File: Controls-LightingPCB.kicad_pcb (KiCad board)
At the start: 2 copper layers, 73.9 x 98.8 mm, 92 parts, among them J1 MinionConn, J10 INTERNAL_RIGHTBLINK, J11 INTERNAL_LEFTBLINK, J12 EXTERNAL_RIGHTBLINK, J13 EXTERNAL_HDLT, J14 EXTERNAL_BRAKELIGHT, J2 12VPWRCONN, J3 CRUZ_ST_INDICATOR_33v, J4 CRUZ_EN_INDICATOR_33v, J5 REGEN_INDICATOR_33v, J6 NEU_INDICATOR_33v, J7 FOR_INDICATOR_33v, J8 REV_INDICATOR_33v, J9 EXTERNAL_LEFTBLINK, Q1 2N7000, Q2 2N7000, Q3 2N7000, Q4 2N7000, Q5 2N7000, SW1 CRUISE_SET, SW2 CRUISE_ENABLE, SW3 F/R_SW, SW4 REGEN_SW, SW5 TURN_SIGNAL_SW, U1 NCP1117-3.3_SOT223

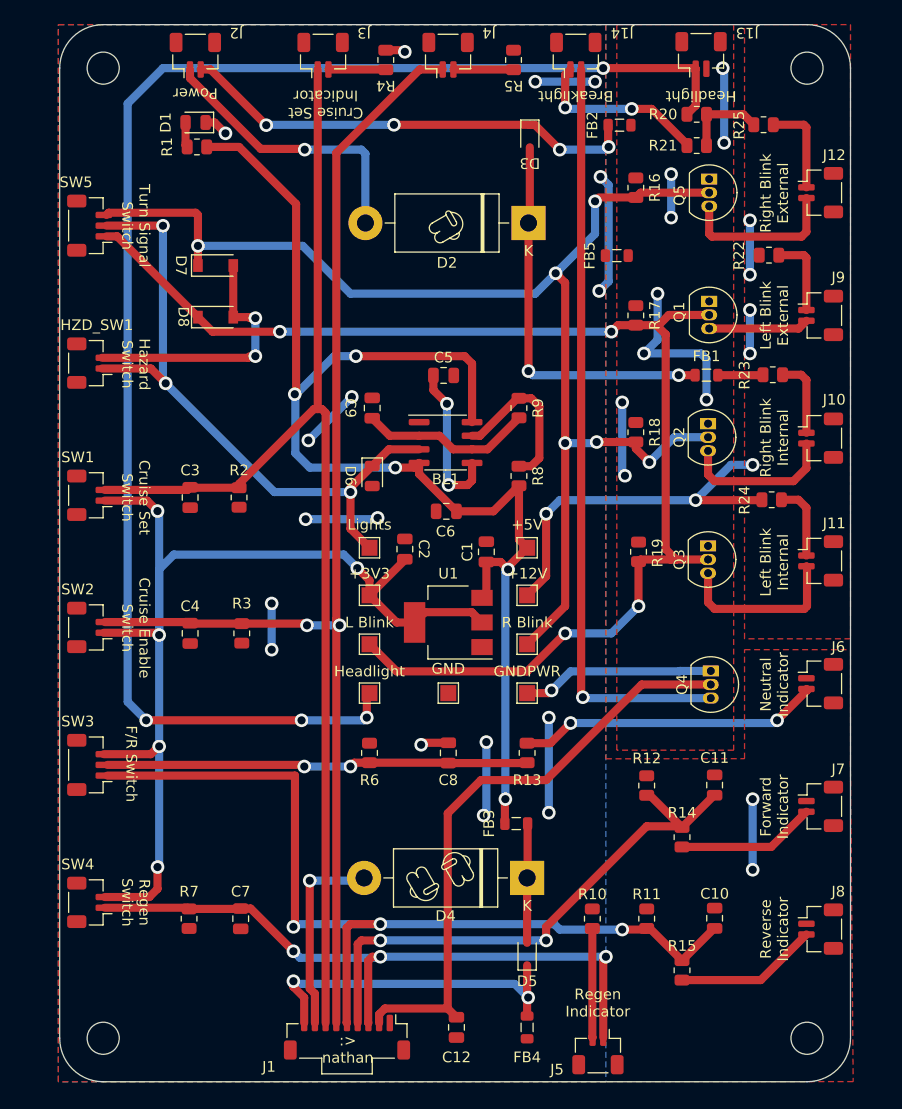
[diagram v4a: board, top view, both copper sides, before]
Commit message: Changed to SMD mosfets
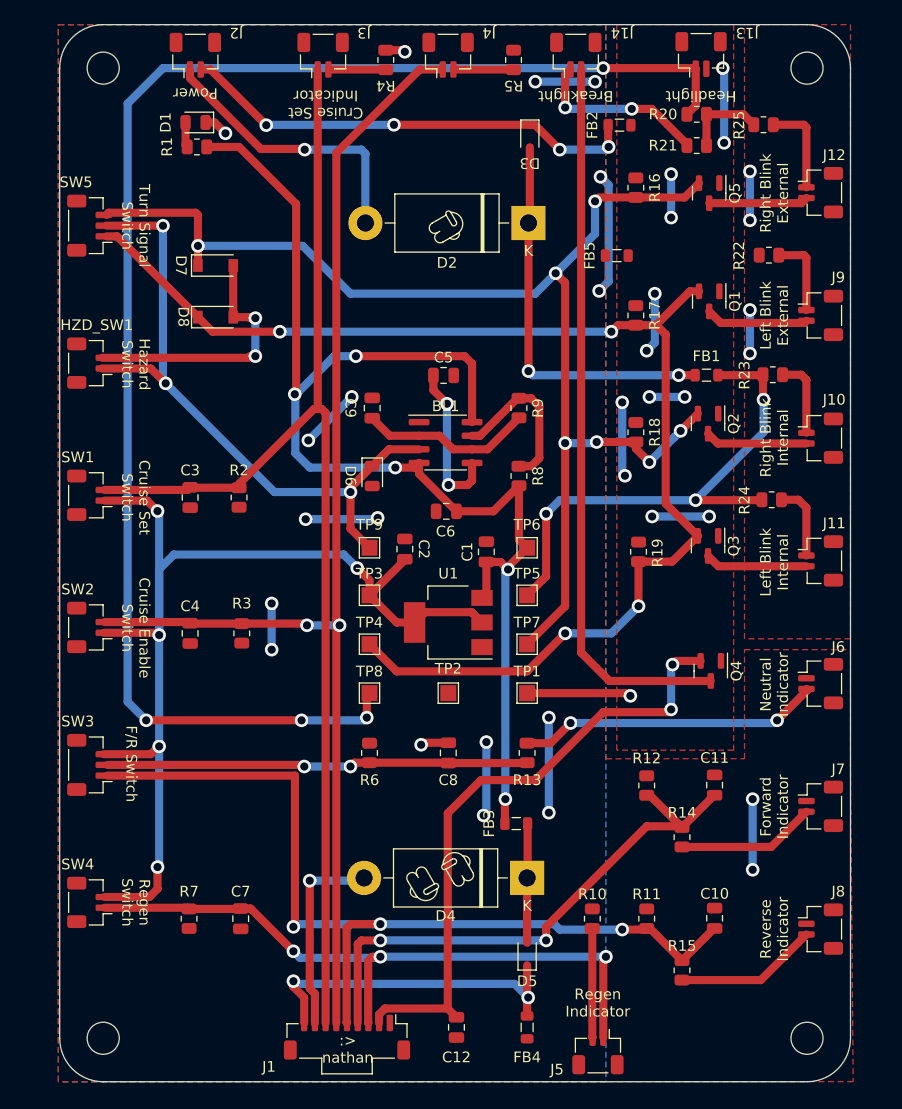
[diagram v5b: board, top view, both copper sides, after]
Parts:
- Q1, Q2, Q3, Q4, Q5: footprint Package_TO_SOT_THT:TO-92_Inline -> Package_TO_SOT_SMD:SOT-23
- TP4: renamed from L Blink
- TP7: renamed from R Blink
- moved Q5 1.31 mm to (168.7, 59.7)
- renumbered GNDPWR to TP1, GND to TP2, +3V3 to TP3, +12V to TP5, +5V to TP6, Headlight to TP8, Lights to TP9
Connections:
- net +3V3 renamed +3.3V
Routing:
- net GNDPWR: track 52.1 -> 42.1 mm, vias 10 -> 13
- net +12V: track 56.8 -> 64.0 mm
- net Net-(J11-Pad2): track 16.1 -> 9.59 mm
- net Net-(J12-Pad2): track 15.1 -> 9.29 mm
- net Net-(J10-Pad2): track 14.5 -> 9.57 mm
- net Net-(J14-Pad2): track 70.7 -> 67.7 mm, vias 1 -> 0
- net /BRAKELIGHT: track 56.4 -> 58.2 mm, vias 0 -> 2
- net /LEFT_BLINK: track 122.7 -> 121.4 mm
- net /RIGHT_BLINK: track 120.3 -> 119.5 mm, vias 6 -> 7

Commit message: updated board
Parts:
- added .: LOGO, UTSVT_Special:kevin, B.Cu at (135.9, 80.9)
- L Blink: renamed from TP4
- R Blink: renamed from TP7
- moved R20 6.01 mm to (162.3, 49.3)
- renumbered TP5 to +12V, TP3 to +3.3V, TP6 to +5V, TP2 to GND, TP1 to GNDPWR, TP8 to Headlights, TP9 to LighsCLK
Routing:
- net GNDPWR: track 42.1 -> 57.5 mm, vias 13 -> 12
- net +12V: track 64.0 -> 70.5 mm
- net Net-(BL1-Pad5): track 14.8 -> 16.4 mm
- net /HEADLIGHT_SW: track 140.6 -> 140.0 mm

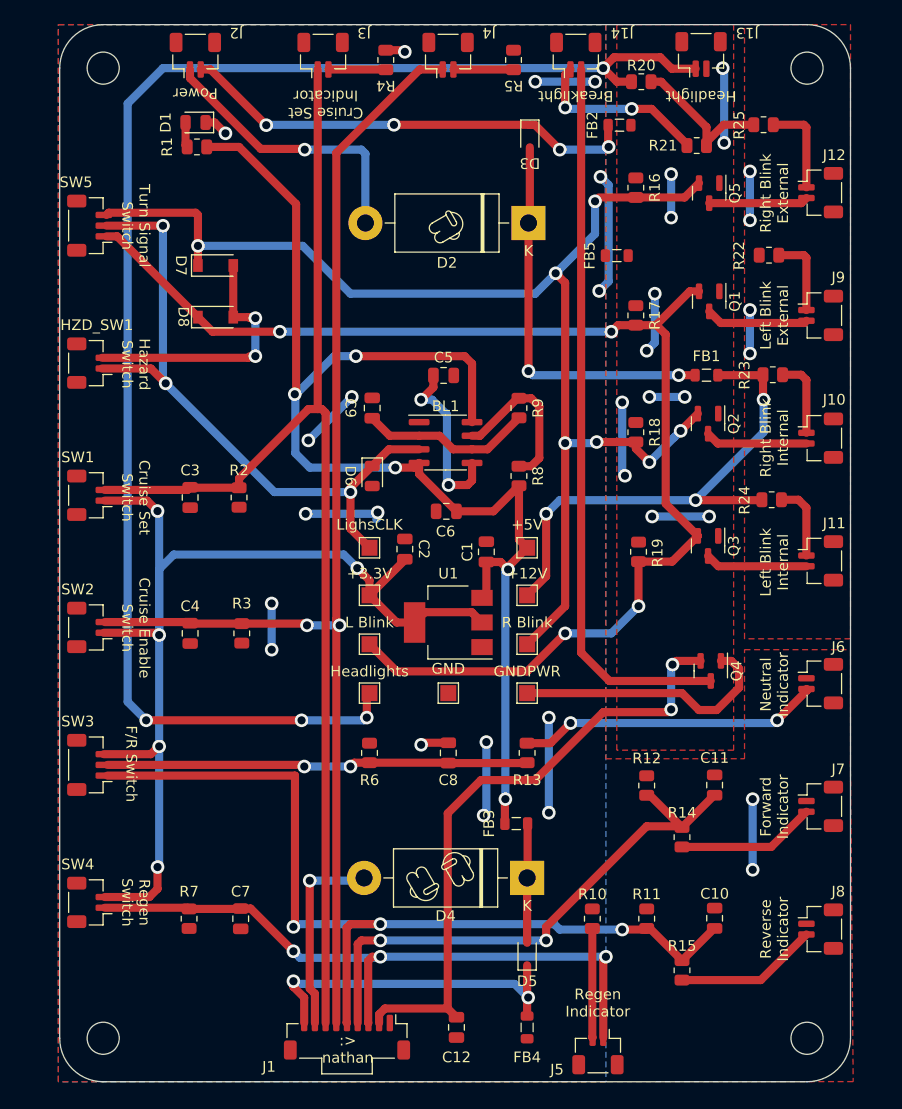
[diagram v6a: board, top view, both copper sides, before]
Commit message: changes to traces and movement of test points
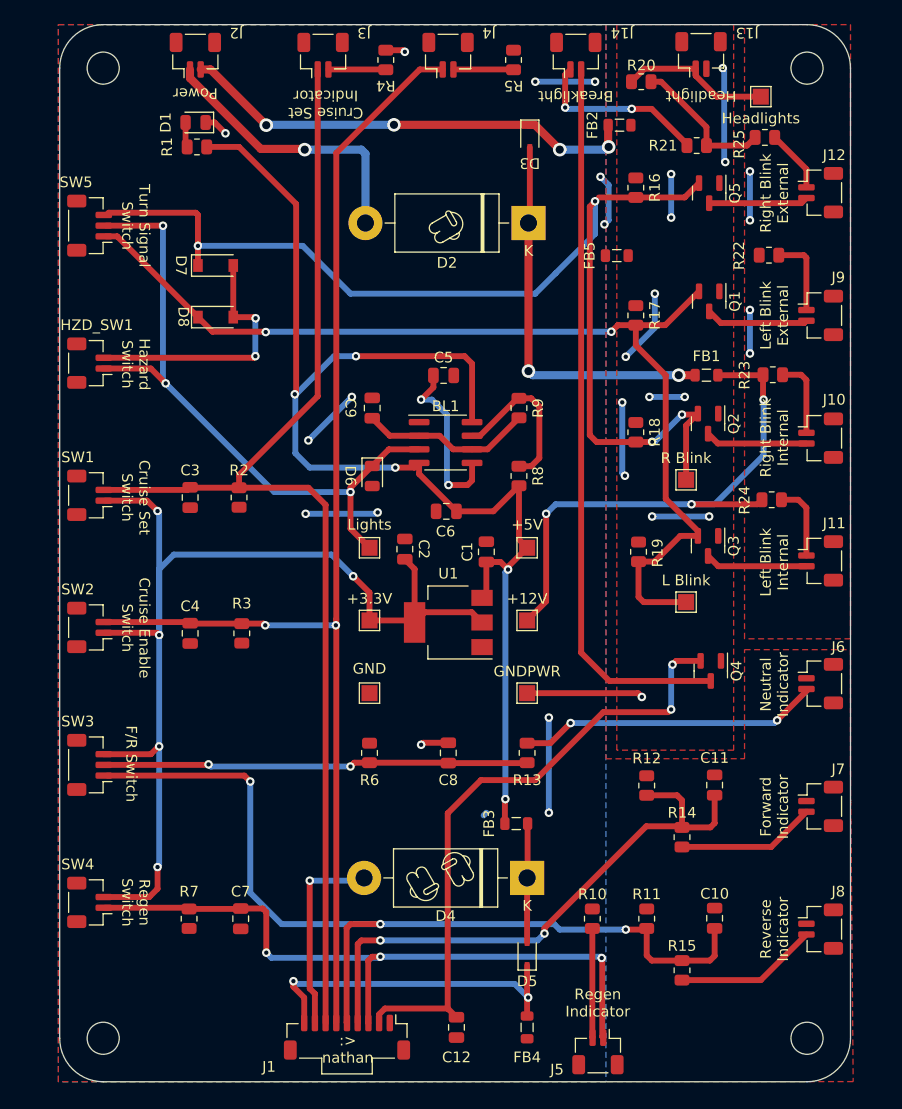
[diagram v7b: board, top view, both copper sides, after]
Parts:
- moved Headlights 66.7 mm to (173.5, 50.7), turned to -90 degrees
- moved L Blink 29.9 mm to (166.5, 97.9)
- moved R Blink 21.4 mm to (166.5, 86.5)
- moved . 16.1 mm to (152.1, 80.7), turned to 165 degrees
- moved GND 7.37 mm to (136.9, 106.4)
- moved +12V 2.35 mm to (151.6, 99.6)
- moved +3.3V 2.35 mm to (136.9, 99.6)
- moved R25 1.19 mm to (173.9, 54.5)
- renumbered LighsCLK to Lights
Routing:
- net /HEADLIGHT_SW: track 140.0 -> 14.1 mm, vias 4 -> 0
- net /LEFT_BLINK: track 121.4 -> 97.3 mm, vias 4 -> 2
- net GND: track 63.2 -> 39.0 mm, vias 19 -> 13
- net /RIGHT_BLINK: track 119.5 -> 107.9 mm, vias 7 -> 4
- net GNDPWR: track 57.5 -> 46.4 mm, vias 12 -> 13
- net +12V: track 70.5 -> 74.0 mm
- net Net-(J12-Pad1): track 8.81 -> 5.89 mm
- net /FOR_SW: track 51.9 -> 54.4 mm
- net +3.3V: track 102.6 -> 105.0 mm
- net /REGEN_SW: track 63.6 -> 65.4 mm
- net /CRUZ_ST: track 113.2 -> 112.0 mm
- net Net-(D7-Pad2): track 23.9 -> 24.9 mm
